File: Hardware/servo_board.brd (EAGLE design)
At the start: 30.5 x 53.3 mm, 33 parts, among them U1 PCA9685, U2 PCA9306, U3 EDISON_CONNECTOR_FULLMOUNTING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, U4 EDISON_CONNECTOR_FULLHEADER

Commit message: Incorporate review changes
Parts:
- added FID1, FID2: FIDUCIALUFIDUCIAL, SparkFun-Aesthetics:MICRO-FIDUCIAL
- added LOGO1: SFE_LOGO_NAME_FLAME.1_INCH, SparkFun-Aesthetics:SFE_LOGO_NAME_FLAME_.1
- added LOGO4: OSHW-LOGOS, SparkFun-Aesthetics:OSHW-LOGO-S
- added R14, R15, R16, R17, R18, R19: 1K, SparkFun-Resistors:0603-RES
- added SJ1, SJ2, SJ3, SJ4, SJ5, SJ6: JUMPER-PAD-2-NOYES_SILK, SparkFun-Passives:PAD-JUMPER-2-NO_YES_SILK
- moved C2 3.81 mm to (17.1, 29.2)
- moved U1 3.81 mm to (11.4, 29.2)
- moved C1 3.24 mm to (10.8, 14.6)
- moved R3 3.24 mm to (12.1, 17.1)
- moved R2 2.62 mm to (12.1, 20.3)
- moved C3 0.38 mm to (8.89, 11.4)
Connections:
- new net A0: R14.2, SJ1.2, U1.1
- new net A1: R15.2, SJ2.2, U1.2
- new net A2: R16.2, SJ3.2, U1.3
- new net A3: R17.2, SJ4.2, U1.4
- new net A4: R18.2, SJ5.2, U1.5
- new net A5: R19.2, SJ6.2, U1.24
- net GND: now also R14.1, R15.1, R16.1, R17.1, R18.1, R19.1; no longer U1.24, U1.4, U1.5
- net VSYS: now also SJ1.1, SJ2.1, SJ3.1, SJ4.1, SJ5.1, SJ6.1
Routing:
- net VSYS: track 33.7 -> 67.1 mm, vias 3 -> 5
- net A0: track 0.00 -> 32.7 mm, vias 0 -> 2
- net A1: track 0.00 -> 29.3 mm, vias 0 -> 2
- net A2: track 0.00 -> 26.7 mm, vias 0 -> 2
- net A3: track 0.00 -> 22.4 mm, vias 0 -> 2
- net A4: track 0.00 -> 19.9 mm, vias 0 -> 2
- net A5: track 0.00 -> 13.6 mm, vias 0 -> 2
- net HV_SCL: track 7.42 -> 11.8 mm
- net HV_SDA: track 7.45 -> 11.3 mm
- net CH7: track 19.2 -> 15.4 mm
- net CH6: track 19.5 -> 15.7 mm
- net CH0: track 29.4 -> 26.1 mm
- net CH5: track 20.3 -> 17.2 mm
- net CH1: track 27.1 -> 24.1 mm
- net CH2: track 23.9 -> 20.9 mm
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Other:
- board text added: "8-Servo Controller Edzzanine"
- board text added: "A0"
- board text added: "A1"
- board text added: "A2"
- board text added: "A3"
- board text added: "A4"
- board text added: "A5"
- board text added: "CH0"
- board text added: "CH1"
- board text added: "CH2"
- board text added: "CH3"
- board text added: "CH4"
- board text added: "CH5"
- board text added: "CH6"
- board text added: "CH7"
- board text removed: "8-Servo Controller"

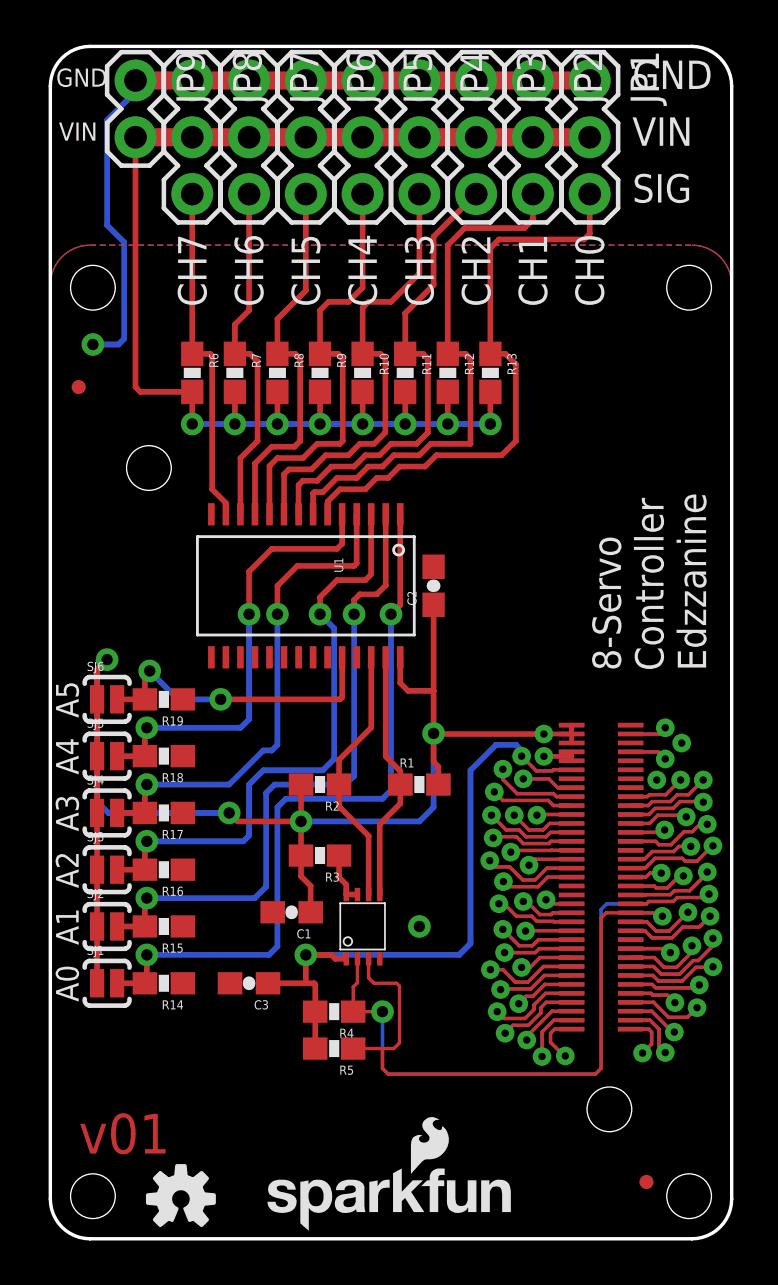
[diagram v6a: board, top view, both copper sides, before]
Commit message: Fix fids, remove weird name
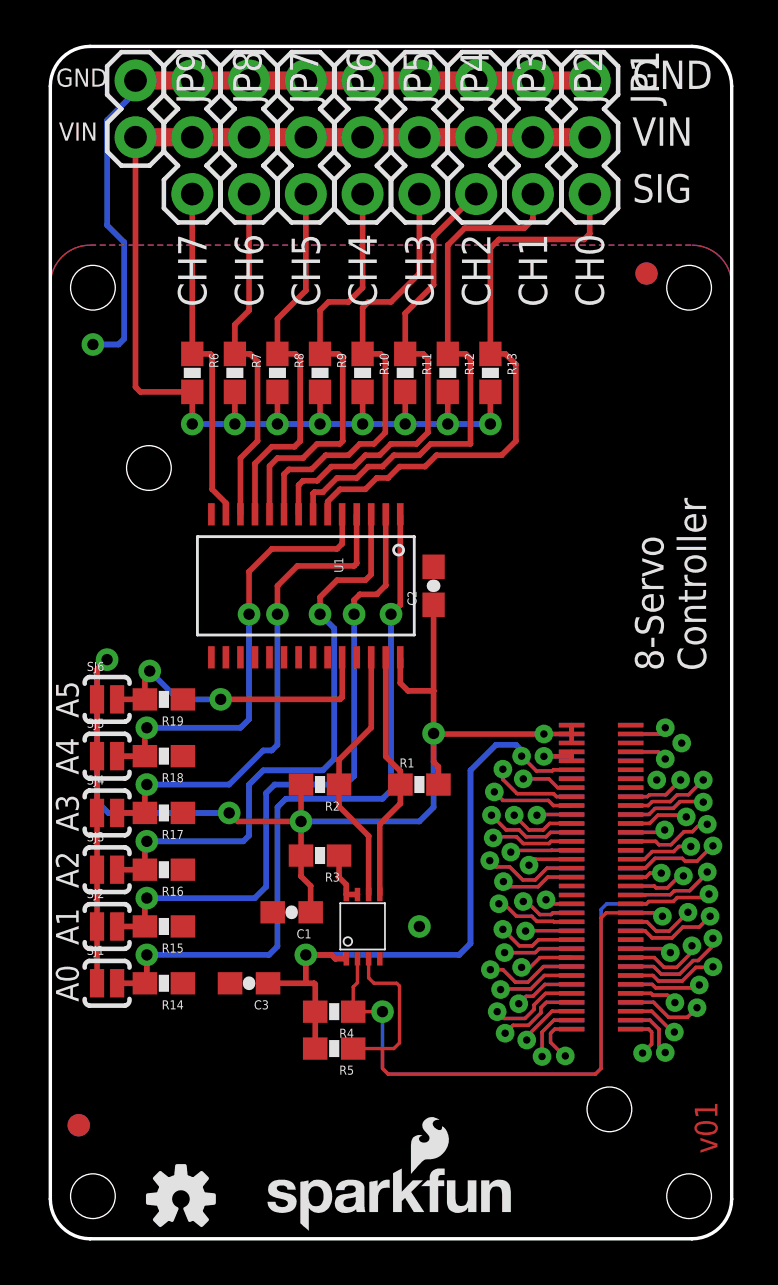
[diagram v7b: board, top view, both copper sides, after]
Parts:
- added FID3, FID4: FIDUCIAL1X2, SparkFun-Aesthetics:FIDUCIAL-1X2
- FID1, FID2: value FIDUCIALUFIDUCIAL -> FIDUCIAL1X2; device SparkFun-Aesthetics:MICRO-FIDUCIAL -> SparkFun-Aesthetics:FIDUCIAL-1X2
- moved FID2 25.9 mm to (26.7, 43.2)
- moved FID1 25.5 mm to (1.27, 5.08)
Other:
- board text added: "8-Servo Controller"
- board text removed: "8-Servo Controller Edzzanine"
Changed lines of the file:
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@@
 <text x="-2.54" y="41.91" size="1.778" layer="51" rot="R270">LED's and selector switches go here</text>
 <text x="31.115" y="39.37" size="1.778" layer="51" rot="R270">Nothing goes here...  I mean it.</text>
-<text x="24.257" y="25.4" size="1.27" layer="22" font="vector" ratio="15" rot="MR90">8-Servo
-Controller
-Edzzanine</text>
+<text x="26.162" y="25.4" size="1.27" layer="22" font="vector" ratio="15" rot="MR90">8-Servo
+Controller</text>
 <wire x1="1.778" y1="53.34" x2="28.702" y2="53.34" width="0.1524" layer="20"/>
 <wire x1="30.48" y1="44.704" x2="30.48" y2="53.34" width="0.254" layer="51"/>
@@
 <dimension x1="29.28210625" y1="41.83789375" x2="27.86789375" y2="43.25210625" x3="34.29" y3="48.26" textsize="1.778" layer="51" dtype="diameter"/>
 <text x="29.21" y="6.35" size="1.016" layer="22" font="vector" ratio="15" rot="MR90" align="center">4xM2.0</text>
-<text x="1.27" y="3.81" size="1.778" layer="1" font="vector" ratio="15">v01</text>
+<text x="29.845" y="3.81" size="1.016" layer="1" font="vector" ratio="15" rot="R90">v01</text>
 <text x="29.21" y="52.07" size="1.27" layer="22" font="vector" ratio="15" rot="MR0" align="center-left">GND</text>
 <text x="29.21" y="49.53" size="1.27" layer="22" font="vector" ratio="15" rot="MR0" align="center-left">VIN</text>
@@
 <text x="26.035" y="46.99" size="1.27" layer="21" font="vector" ratio="15" align="center-left">SIG</text>
 <text x="29.337" y="25.4" size="1.27" layer="21" font="vector" ratio="15" rot="R90">8-Servo
-Controller
-Edzzanine</text>
+Controller</text>
 <text x="0.254" y="51.943" size="0.8128" layer="21" font="vector" ratio="15" align="center-left">GND</text>
 <text x="0.381" y="49.53" size="0.8128" layer="21" font="vector" ratio="15" align="center-left">VIN</text>
@@
 <element name="LOGO1" library="SparkFun-Aesthetics" package="SFE_LOGO_NAME_FLAME_.1" value="SFE_LOGO_NAME_FLAME.1_INCH" x="9.271" y="0.254"/>
 <element name="LOGO4" library="SparkFun-Aesthetics" package="OSHW-LOGO-S" value="OSHW-LOGOS" x="5.842" y="1.778"/>
-<element name="FID1" library="SparkFun-Aesthetics" package="MICRO-FIDUCIAL" value="FIDUCIALUFIDUCIAL" x="26.67" y="2.54"/>
-<element name="FID2" library="SparkFun-Aesthetics" package="MICRO-FIDUCIAL" value="FIDUCIALUFIDUCIAL" x="1.27" y="38.1"/>
+<element name="FID1" library="SparkFun-Aesthetics" package="FIDUCIAL-1X2" value="FIDUCIAL1X2" x="1.27" y="5.08"/>
+<element name="FID2" library="SparkFun-Aesthetics" package="FIDUCIAL-1X2" value="FIDUCIAL1X2" x="26.67" y="43.18"/>
 <element name="R14" library="SparkFun-Resistors" package="0603-RES" value="1K" x="5.08" y="11.43" rot="R180">
 <attribute name="PROD_ID" value="RES-07856" x="5.08" y="11.43" size="1.778" layer="27" font="vector" ratio="15" rot="R180" display="off"/>
@@
 <element name="SJ5" library="SparkFun-Passives" package="PAD-JUMPER-2-NO_YES_SILK" value="JUMPER-PAD-2-NOYES_SILK" x="2.54" y="21.59"/>
 <element name="SJ6" library="SparkFun-Passives" package="PAD-JUMPER-2-NO_YES_SILK" value="JUMPER-PAD-2-NOYES_SILK" x="2.54" y="24.13"/>
+<element name="FID3" library="SparkFun-Aesthetics" package="FIDUCIAL-1X2" value="FIDUCIAL1X2" x="1.27" y="5.08" rot="MR0"/>
+<element name="FID4" library="SparkFun-Aesthetics" package="FIDUCIAL-1X2" value="FIDUCIAL1X2" x="26.67" y="43.18" rot="MR0"/>
 </elements>
 <signals>
